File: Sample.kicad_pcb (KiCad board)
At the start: 2 copper layers, 108 parts

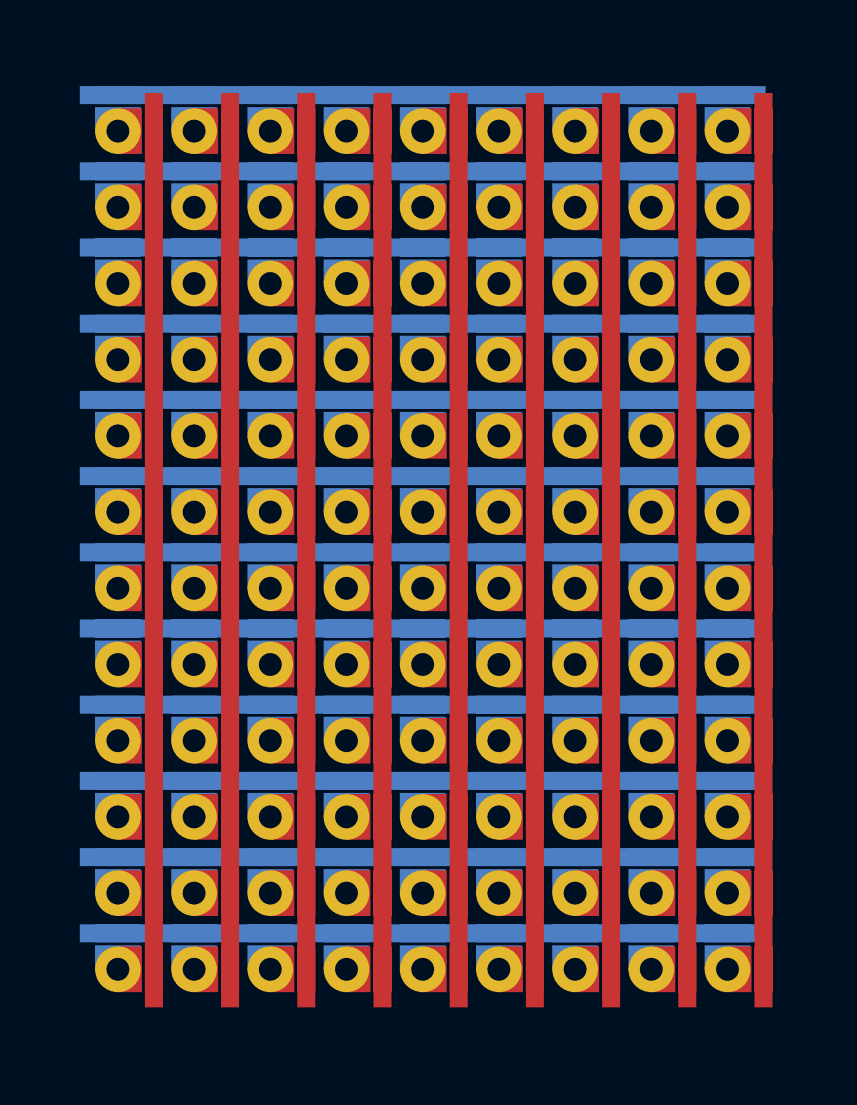
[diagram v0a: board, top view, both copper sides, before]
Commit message: Edge cuts for the sample
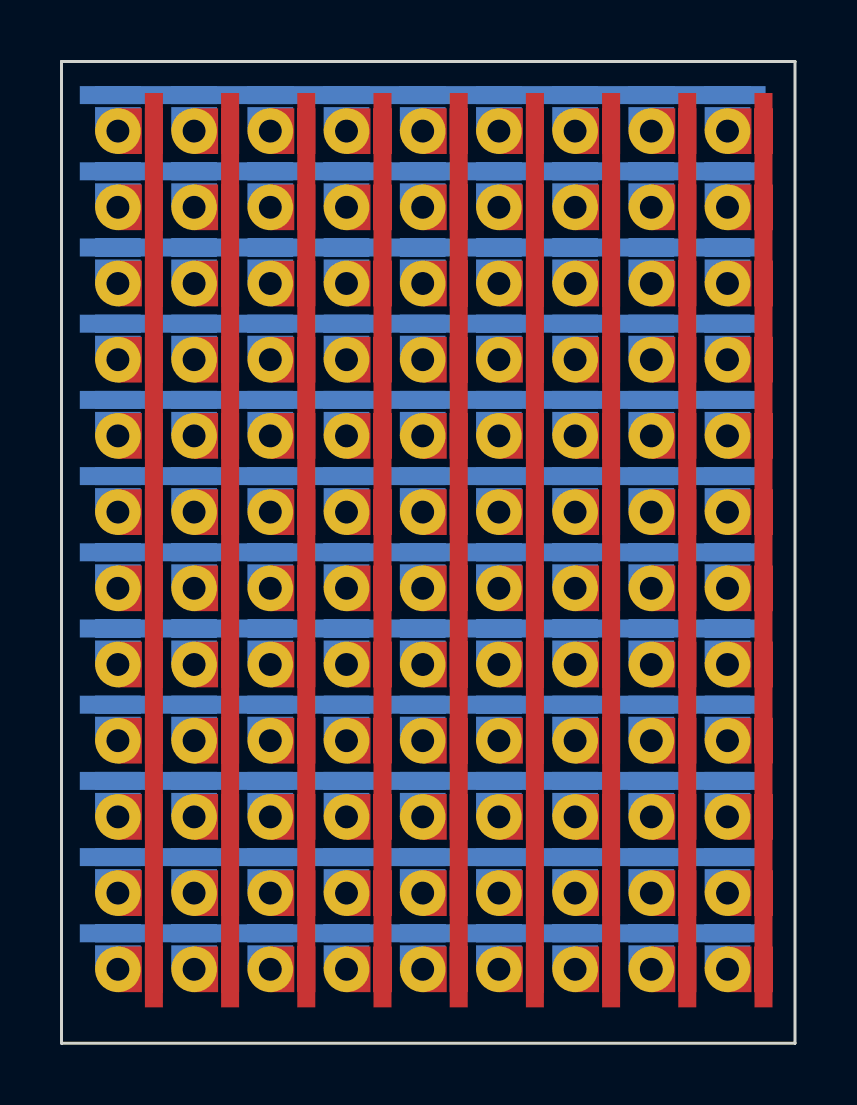
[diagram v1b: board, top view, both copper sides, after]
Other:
- board outline added: 24.4 x 32.7 mm
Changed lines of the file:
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@@
     (pad "3" smd rect (at 0 -1.2 90) (size 0.6 2.54) (layers "B.Cu"))
   )
+  (gr_rect (start 142.9 56.1) (end 167.35 88.825)
+    (stroke (width 0.1) (type default)) (fill none) (layer "Edge.Cuts"))
 )
